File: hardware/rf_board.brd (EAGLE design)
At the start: 109.9 x 68.6 mm, 31 parts, among them IC1 LM358MX, X3 KUSBVX

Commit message: RF board update
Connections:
- removed net SCL: U$1.2
- removed net SDA: U$1.1
- net SCL1: now also U$1.2
- net SDA1: now also U$1.1
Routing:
- net SDA1: track 0.00 -> 72.8 mm, vias 0 -> 2
- net SCL1: track 0.00 -> 72.6 mm, vias 0 -> 2
- net SCL: track 71.1 -> 0.00 mm, vias 2 -> 0
- net SDA: track 70.6 -> 0.00 mm, vias 2 -> 0
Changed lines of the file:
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@@
 <contactref element="SV1" pad="3"/>
 <contactref element="JP2" pad="4"/>
+<contactref element="U$1" pad="2"/>
+<via x="59.055" y="55.5766" extent="1-16" drill="0.6" diameter="1.4224" shape="octagon"/>
+<wire x1="59.055" y1="55.5766" x2="61.881" y2="55.5766" width="0.6096" layer="16"/>
+<via x="96.901" y="55.5766" extent="1-16" drill="0.6" diameter="1.4224" shape="octagon"/>
+<wire x1="96.901" y1="55.5766" x2="96.901" y2="29.3116" width="0.4064" layer="16"/>
+<wire x1="96.901" y1="29.3116" x2="93.9292" y2="26.3398" width="0.4064" layer="16"/>
+<wire x1="59.055" y1="55.5766" x2="96.901" y2="55.5766" width="0.4064" layer="1"/>
+<wire x1="93.9292" y1="24.8666" x2="93.9292" y2="26.3398" width="0.4064" layer="16"/>
 <wire x1="63.119" y1="12.065" x2="93.9292" y2="24.8666" width="0" layer="19" extent="1-1"/>
 </signal>
@@
 <contactref element="SV1" pad="6"/>
 <contactref element="JP2" pad="3"/>
+<contactref element="U$1" pad="1"/>
+<via x="59.055" y="53.5766" extent="1-16" drill="0.6" diameter="1.4224" shape="octagon"/>
+<wire x1="59.055" y1="53.5766" x2="61.881" y2="53.5766" width="0.6096" layer="16"/>
+<via x="98.0948" y="54.3306" extent="1-16" drill="0.6" diameter="1.4224" shape="octagon"/>
+<wire x1="98.0948" y1="54.3306" x2="98.0948" y2="28.6004" width="0.4064" layer="16"/>
+<wire x1="98.0948" y1="28.6004" x2="96.4692" y2="26.9748" width="0.4064" layer="16"/>
+<wire x1="98.0948" y1="54.3306" x2="96.4184" y2="54.3306" width="0.4064" layer="1"/>
+<wire x1="96.4184" y1="54.3306" x2="95.885" y2="54.864" width="0.4064" layer="1"/>
+<wire x1="95.885" y1="54.864" x2="60.3424" y2="54.864" width="0.4064" layer="1"/>
+<wire x1="60.3424" y1="54.864" x2="59.055" y2="53.5766" width="0.4064" layer="1"/>
+<wire x1="96.4692" y1="24.8666" x2="96.4692" y2="26.9748" width="0.4064" layer="16"/>
 <wire x1="65.659" y1="9.525" x2="96.4692" y2="24.8666" width="0" layer="19" extent="1-1"/>
 </signal>
@@
 <wire x1="80.5948" y1="64.7198" x2="80.645" y2="64.77" width="0.34798125" layer="16"/>
 </signal>
-<signal name="SDA">
-<contactref element="U$1" pad="1"/>
-<via x="59.055" y="53.5766" extent="1-16" drill="0.6" diameter="1.4224" shape="octagon"/>
-<wire x1="59.055" y1="53.5766" x2="61.881" y2="53.5766" width="0.6096" layer="16"/>
-<via x="98.0948" y="54.3306" extent="1-16" drill="0.6" diameter="1.4224" shape="octagon"/>
-<wire x1="98.0948" y1="54.3306" x2="98.0948" y2="28.6004" width="0.4064" layer="16"/>
-<wire x1="98.0948" y1="28.6004" x2="96.4692" y2="26.9748" width="0.4064" layer="16"/>
-<wire x1="98.0948" y1="54.3306" x2="96.4184" y2="54.3306" width="0.4064" layer="1"/>
-<wire x1="96.4184" y1="54.3306" x2="95.885" y2="54.864" width="0.4064" layer="1"/>
-<wire x1="95.885" y1="54.864" x2="60.3424" y2="54.864" width="0.4064" layer="1"/>
-<wire x1="60.3424" y1="54.864" x2="59.055" y2="53.5766" width="0.4064" layer="1"/>
-</signal>
-<signal name="SCL">
-<contactref element="U$1" pad="2"/>
-<via x="59.055" y="55.5766" extent="1-16" drill="0.6" diameter="1.4224" shape="octagon"/>
-<wire x1="59.055" y1="55.5766" x2="61.881" y2="55.5766" width="0.6096" layer="16"/>
-<via x="96.901" y="55.5766" extent="1-16" drill="0.6" diameter="1.4224" shape="octagon"/>
-<wire x1="96.901" y1="55.5766" x2="96.901" y2="29.3116" width="0.4064" layer="16"/>
-<wire x1="96.901" y1="29.3116" x2="93.9292" y2="26.3398" width="0.4064" layer="16"/>
-<wire x1="59.055" y1="55.5766" x2="96.901" y2="55.5766" width="0.4064" layer="1"/>
-</signal>
 <signal name="CLK2">

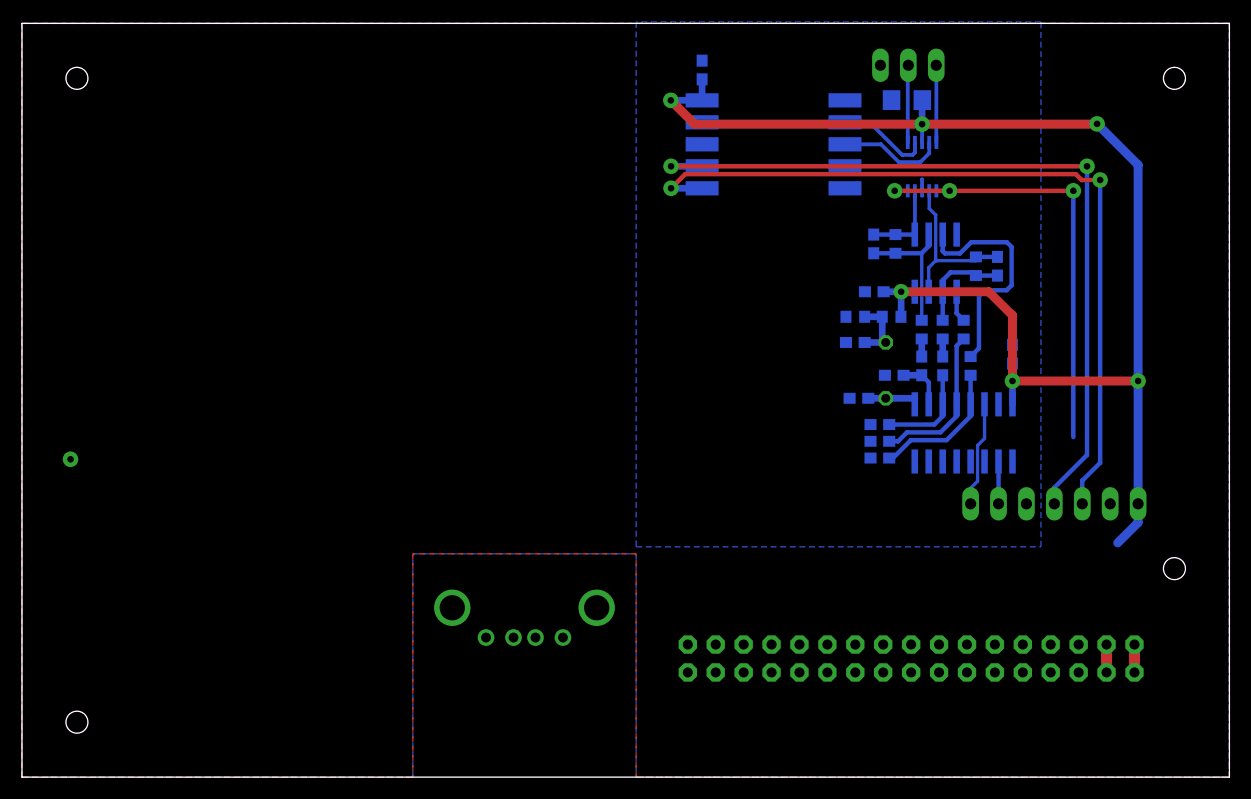
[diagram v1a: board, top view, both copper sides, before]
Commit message: RF board updated
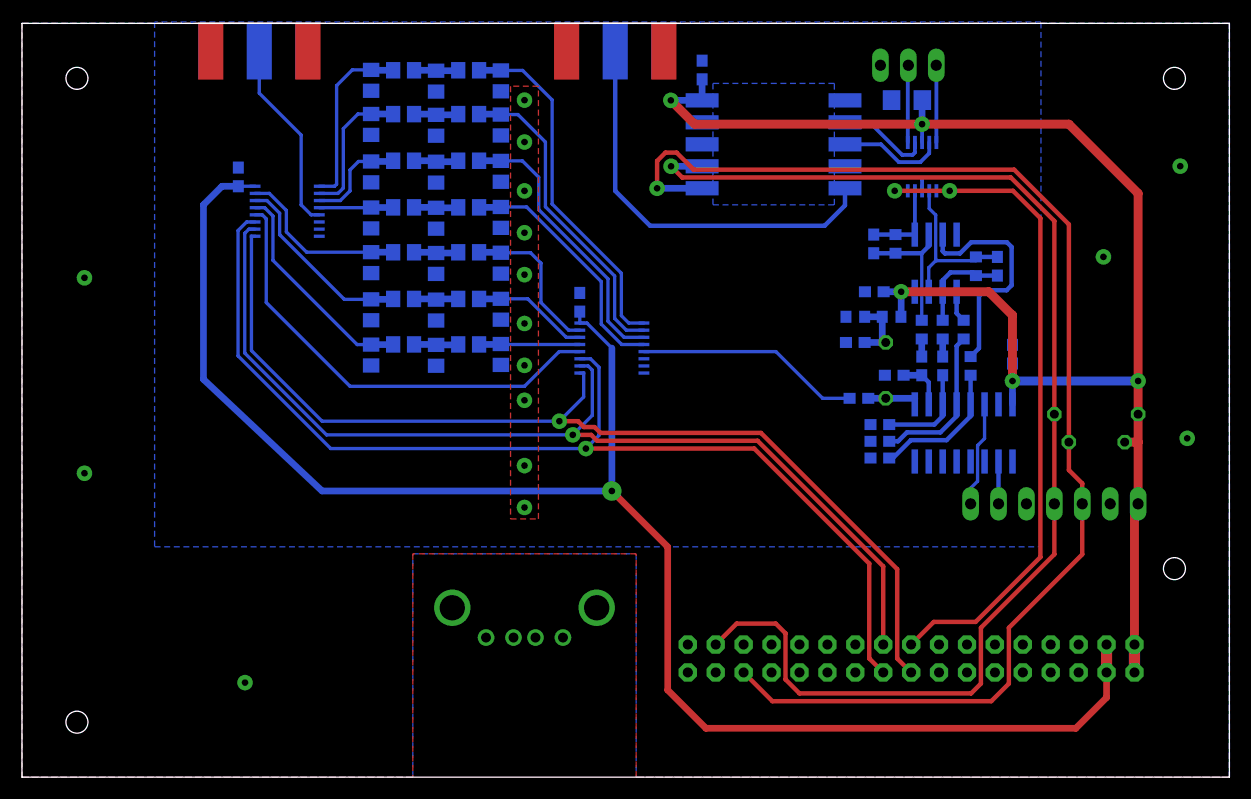
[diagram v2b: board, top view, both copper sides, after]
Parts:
- added C15, C16, C17, C18, C19, C20, C21, C22, C23, C24, C25, C26, C27, C28, C29, C30, C31, C32, C33, C34, C35: (no value), rcl:C0805
- added C36, C37: 100n, rcl:C0603
- added L1, L10, L11, L12, L13, L14, L2, L3, L4, L5, L6, L7, L8, L9: (no value), rcl:R0805
- added R10: (no value), rcl:0204/7
- added R11: (no value), rcl:0204/5
- added U$4, U$5: SN74CBT3251, mw:TSSOP16
- added X1, X2: SMA-142-0701-801/806, con-coax:J502-ND-142-0701-801/806
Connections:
- removed net N$12: U$2.1, U$2.5
- removed net RD7: SV1.16
- removed net RG0: SV1.18
- removed net RG1: SV1.15
- new net LPF_16_30_A: C17.1, L2.1, U$5.1
- new net LPF_16_30_B: C16.1, L1.2, U$4.1
- new net LPF_1_2_A: C29.1, L10.1, U$5.15
- new net LPF_1_2_B: C28.1, L9.2, U$4.15
- new net LPF_250K_A: C35.1, L14.1, U$5.13
- new net LPF_250K_B: C34.1, L13.2, U$4.13
- new net LPF_2_4_A: C26.1, L8.1, U$5.4
- new net LPF_2_4_B: C25.1, L7.2, U$4.4
- new net LPF_4_8_A: C23.1, L6.1, U$5.3
- new net LPF_4_8_B: C22.1, L5.2, U$4.3
- new net LPF_500K_1_A: C32.1, L12.1, U$5.14
- new net LPF_500K_1_B: C31.1, L11.2, U$4.14
- new net LPF_8_16_A: C20.1, L4.1, U$5.2
- new net LPF_8_16_B: C19.1, L3.2, U$4.2
- new net N$19: C15.1, L1.1, L2.2
- new net N$20: U$5.5, X2.1
- new net N$21: U$1.10, X1.1
- new net N$22: C18.1, L3.1, L4.2
- new net N$25: C21.1, L5.1, L6.2
- new net N$28: C24.1, L7.1, L8.2
- new net N$31: C27.1, L10.2, L9.1
- new net N$34: C30.1, L11.1, L12.2
- new net N$38: C33.1, L13.1, L14.2
- new net N$41: C9.1, U$4.5
- new net NO_LPF: U$4.12, U$5.12
- new net RD7_BAND_A0: SV1.16, U$4.11, U$5.11
- new net RG0_BAND_A2: SV1.18, U$4.9, U$5.9
- new net RG1_BAND_A1: SV1.15, U$4.10, U$5.10
- net 3V: now also R10.2, R11.2
- net RA6: now also U$2.1, U$2.5
- net SCL1: now also R10.1
- net SDA1: now also R11.1
- net VBUS: now also C36.1, C37.1, U$4.16, U$5.16
- net VS_AGND: now also C15.2, C16.2, C17.2, C18.2, C19.2, C20.2, C21.2, C22.2, C23.2, C24.2, C25.2, C26.2, C27.2, C28.2, C29.2, C30.2, C31.2, C32.2, C33.2, C34.2, C35.2, C36.2, C37.2, U$4.7, U$4.8, U$5.7, U$5.8, X1.G@1, X1.G@2, X1.G@3, X1.G@4, X2.G@1, X2.G@2, X2.G@3, X2.G@4
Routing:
- net VBUS: track 2.54 -> 147.9 mm, vias 0 -> 1
- net RD7_BAND_A0: track 0.00 -> 98.9 mm, vias 0 -> 1
- net RG0_BAND_A2: track 0.00 -> 93.3 mm, vias 0 -> 1
- net RG1_BAND_A1: track 0.00 -> 93.2 mm, vias 0 -> 1
- net RA6: track 0.00 -> 62.6 mm, vias 0 -> 2
- net SDA1: track 72.8 -> 118.0 mm, vias 2 -> 1
- net SCL1: track 72.6 -> 115.0 mm, vias 2 -> 1
- net NO_LPF: track 0.00 -> 41.8 mm
- net N$12: track 41.1 -> 0.00 mm, vias 3 -> 0
- net N$21: track 0.00 -> 37.2 mm
- net LPF_16_30_B: track 0.00 -> 32.3 mm
- net LPF_8_16_B: track 0.00 -> 28.9 mm
- net LPF_4_8_B: track 0.00 -> 25.6 mm
- net LPF_2_4_B: track 0.00 -> 22.5 mm
- net N$41: track 0.00 -> 20.5 mm
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- added copper zone on layer 16, net N$12
- added copper zone on layer 1, net VS_AGND
